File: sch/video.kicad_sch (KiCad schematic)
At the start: 14 parts

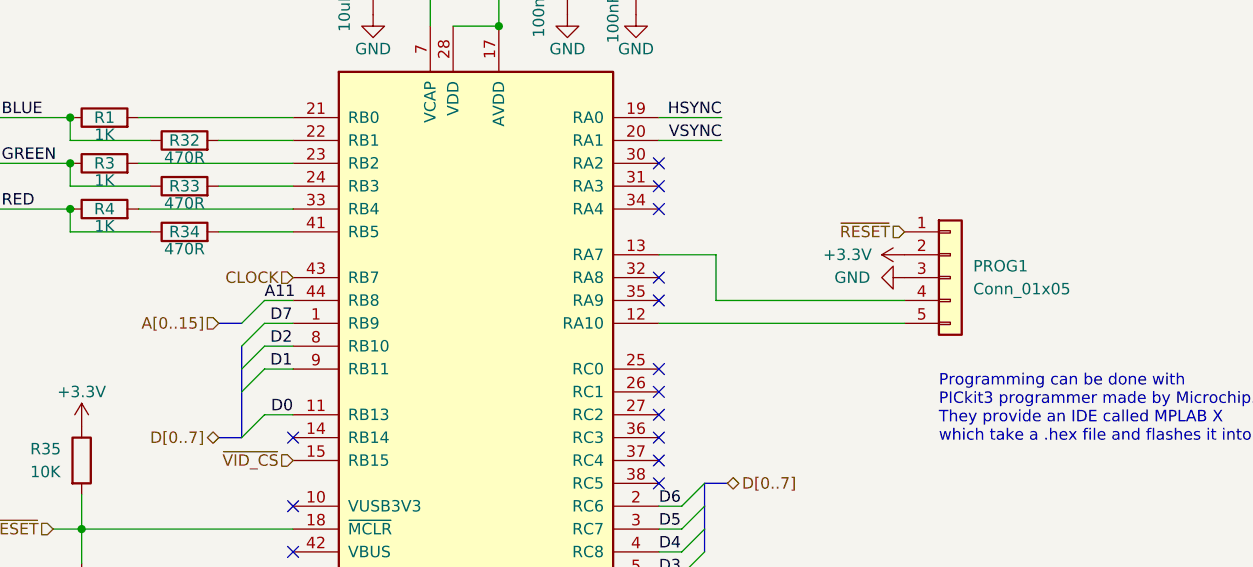
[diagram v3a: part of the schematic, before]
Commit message: bigger header pins
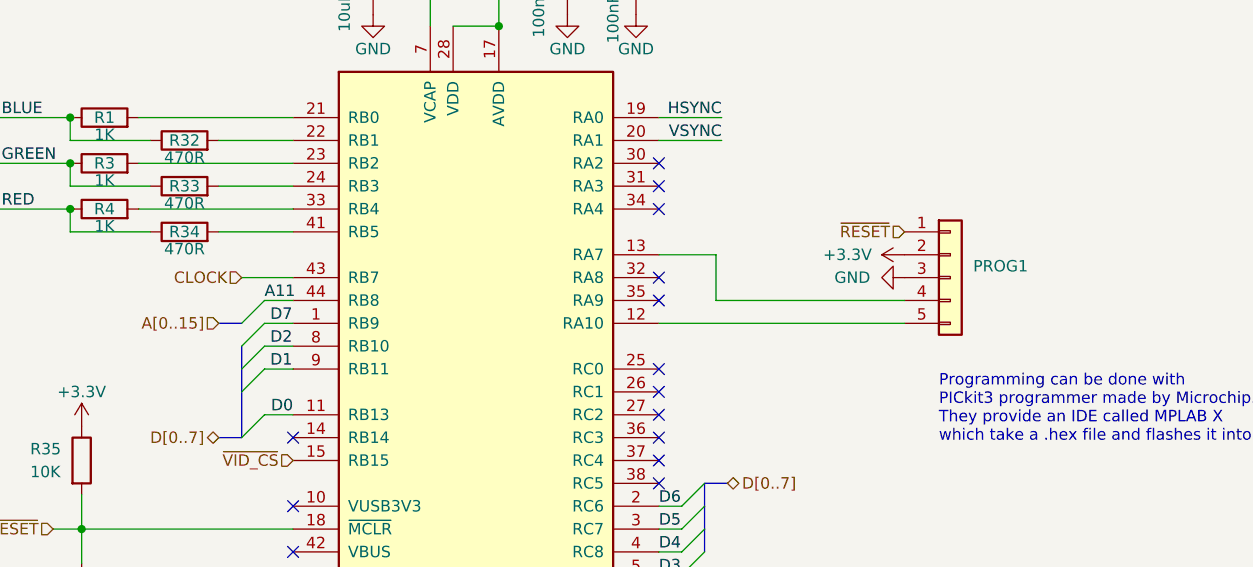
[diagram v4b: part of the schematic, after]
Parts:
- PROG1: value Conn_01x05 -> (none); footprint Connector_PinHeader_2.00mm:PinHeader_1x05_P2.00mm_Vertical -> (none)
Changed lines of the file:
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@@
+    (stroke (width 0) (type default) (color 0 0 0 0))
+  )
+  (wire (pts (xy 110.49 100.33) (xy 116.205 100.33))
     (stroke (width 0) (type default) (color 0 0 0 0))
   )
@@
     (effects (font (size 1.27 1.27)) (justify left bottom))
   )
-  (hierarchical_label "CLOCK" (shape input) (at 116.205 100.33 180)
+  (hierarchical_label "CLOCK" (shape input) (at 110.49 100.33 180)
     (effects (font (size 1.27 1.27)) (justify right))
   )
@@
       (effects (font (size 1.27 1.27)) (justify left))
     )
-    (property "Value" "Conn_01x05" (id 1) (at 191.77 101.5999 0)
-      (effects (font (size 1.27 1.27)) (justify left))
-    )
-    (property "Footprint" "Connector_PinHeader_2.00mm:PinHeader_1x05_P2.00mm_Vertical" (id 2) (at 189.23 100.33 0)
-      (effects (font (size 1.27 1.27)) hide)
-    )
+    (property "Value" "" (id 1) (at 191.77 101.5999 0)
+      (effects (font (size 1.27 1.27)) (justify left))
+    )
+    (property "Footprint" "" (id 2) (at 189.23 100.33 0)
+      (effects (font (size 1.27 1.27)) hide)
+    )

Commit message: small updates
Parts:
- PROG1: value (none) -> Conn_01x05; footprint (none) -> Connector_PinHeader_2.54mm:PinHeader_1x05_P2.54mm_Vertical
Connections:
- net ~{RESET} renamed ~{MCLR}
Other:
- note added: "Video will be generated using a microcontroller which is fast enough to generate the VGA timing signals. CPU will send a single byte to the MCU which can be be a char code or index of glyph, and the MCU just generates the video signal. This setup is limited in generating graphics but it avoids having to keep a large framebuffer in system memory."
- note removed: "Video will be generated using a microcontroller which is fast enough to generate the VGA timing signals. CPU will send a single byte to the MCU which can be be a char code or index of glyph, and the MCU just generates the video signal. This setup is limited in generating graphics but it avoids having to keep a large framebuffer."
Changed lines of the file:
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@@
-    (stroke (width 0) (type default) (color 0 0 0 0))
-  )
-  (wire (pts (xy 89.535 128.27) (xy 92.71 128.27))
     (stroke (width 0) (type default) (color 0 0 0 0))
   )
@@
     (stroke (width 0) (type default) (color 0 0 0 0))
   )
+  (wire (pts (xy 178.435 95.25) (xy 184.15 95.25))
+    (stroke (width 0) (type default) (color 0 0 0 0))
+  )
   (wire (pts (xy 80.645 80.01) (xy 80.645 74.93))
     (stroke (width 0) (type default) (color 0 0 0 0))
@@
   (wire (pts (xy 146.685 63.5) (xy 154.305 63.5))
     (stroke (width 0) (type default) (color 0 0 0 0))
+  )
+  (text "Video Controller" (at 31.75 26.035 0)
+    (effects (font (size 2 2) (thickness 0.254) bold) (justify left bottom))
   )
   (text "0x4800 - 0x480F" (at 31.75 28.575 0)
@@
     (effects (font (size 1.27 1.27)) (justify left bottom))
   )
-  (text "Video will be generated using a \nmicrocontroller which is fast enough to \ngenerate the VGA timing signals.\n\nCPU will send a single byte to the MCU which can\nbe be a char code or index of glyph, and the MCU\njust generates the video signal.\n\nThis setup is limited in generating graphics but\nit avoids having to keep a large framebuffer."
-    (at 31.75 52.705 0)
-    (effects (font (size 1.27 1.27)) (justify left bottom))
-  )
-  (text "Video Controller" (at 31.75 25.4 0)
-    (effects (font (size 2 2) (thickness 0.4) bold) (justify left bottom))
+  (text "Video will be generated using a \nmicrocontroller which is fast enough to \ngenerate the VGA timing signals.\n\nCPU will send a single byte to the MCU which can\nbe be a char code or index of glyph, and the MCU\njust generates the video signal.\n\nThis setup is limited in generating graphics but\nit avoids having to keep a large framebuffer\nin system memory."
+    (at 31.75 53.975 0)
+    (effects (font (size 1.27 1.27)) (justify left bottom))
   )
   (label "RED" (at 83.82 92.71 0)
@@
     (effects (font (size 1.27 1.27)) (justify left bottom))
   )
+  (label "~{MCLR}" (at 100.965 128.27 0)
+    (effects (font (size 1.27 1.27)) (justify left bottom))
+  )
   (label "VSYNC" (at 163.83 85.09 180)
     (effects (font (size 1.27 1.27)) (justify right bottom))
@@
     (effects (font (size 1.27 1.27)) (justify left bottom))
   )
+  (label "~{MCLR}" (at 178.435 95.25 0)
+    (effects (font (size 1.27 1.27)) (justify left bottom))
+  )
   (hierarchical_label "CLOCK" (shape input) (at 110.49 100.33 180)
     (effects (font (size 1.27 1.27)) (justify right))
@@
   (hierarchical_label "D[0..7]" (shape bidirectional) (at 164.465 123.19 0)
     (effects (font (size 1.27 1.27)) (justify left))
-  )
-  (hierarchical_label "~{RESET}" (shape input) (at 89.535 128.27 180)
-    (effects (font (size 1.27 1.27)) (justify right))
-  )
-  (hierarchical_label "~{RESET}" (shape input) (at 184.15 95.25 180)
-    (effects (font (size 1.27 1.27)) (justify right))
   )
   (hierarchical_label "A[0..15]" (shape input) (at 107.95 105.41 180)
@@
       (effects (font (size 1.27 1.27)) (justify left))
     )
-    (property "Value" "" (id 1) (at 191.77 101.5999 0)
-      (effects (font (size 1.27 1.27)) (justify left))
-    )
-    (property "Footprint" "" (id 2) (at 189.23 100.33 0)
-      (effects (font (size 1.27 1.27)) hide)
-    )
+    (property "Value" "Conn_01x05" (id 1) (at 191.77 101.5999 0)
+      (effects (font (size 1.27 1.27)) (justify left))
+    )
+    (property "Footprint" "Connector_PinHeader_2.54mm:PinHeader_1x05_P2.54mm_Vertical" (id 2) (at 189.23 100.33 0)
+      (effects (font (size 1.27 1.27)) hide)
+    )

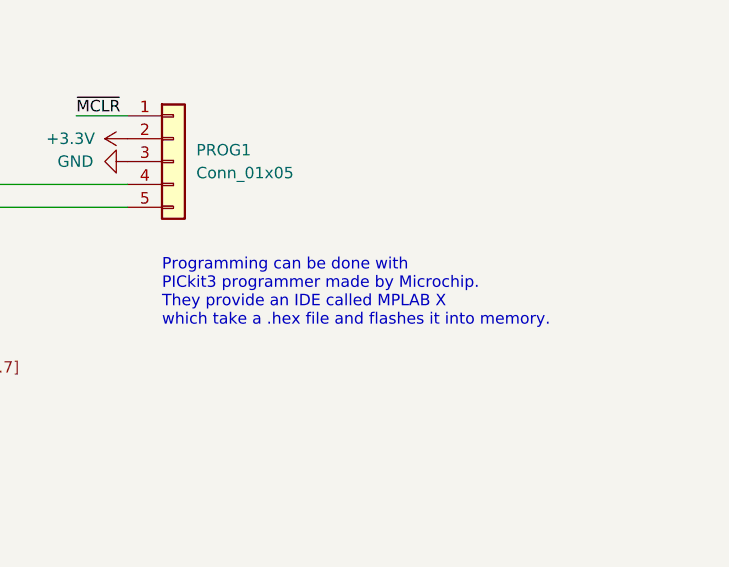
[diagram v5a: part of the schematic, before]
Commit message: Comments in Sch
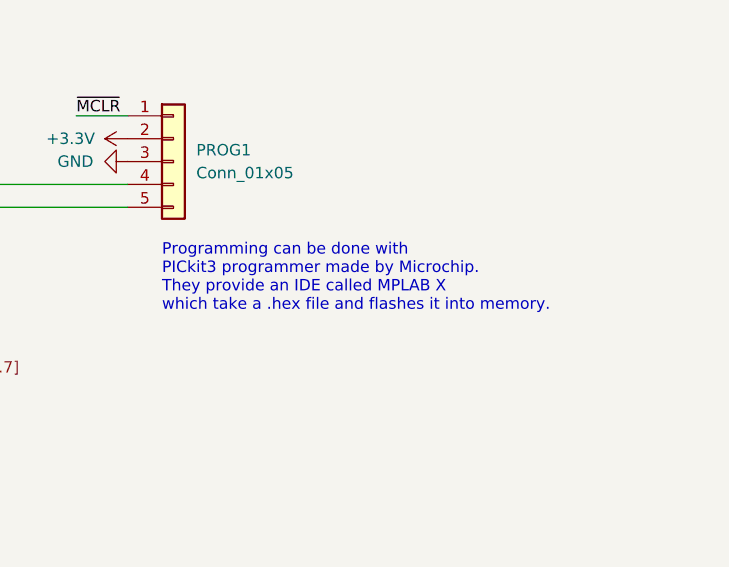
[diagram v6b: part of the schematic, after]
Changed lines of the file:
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@@
     (rev "1.0")
     (company "zrthxn")
+    (comment 1 "https://github.com/zrthxn/8puter")
+    (comment 2 "Open Source Hardware Project")
+    (comment 3 "Homebrew 8-Bit Computer")
   )
   (junction (at 80.645 74.93) (diameter 0) (color 0 0 0 0)
@@
   )
   (text "Programming can be done with\nPICkit3 programmer made by Microchip.\nThey provide an IDE called MPLAB X\nwhich take a .hex file and flashes it into memory."
-    (at 187.96 118.745 0)
+    (at 187.96 117.094 0)
     (effects (font (size 1.27 1.27)) (justify left bottom))
   )

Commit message: nicer label
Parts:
- VGA1: value DB15_Female_HighDensity -> (none); footprint Connector_Dsub:DSUB-15-HD_Female_Horizontal_P2.29x1.98mm_EdgePinOffset3.03mm_Housed_MountingHolesOffset4.94mm -> (none)
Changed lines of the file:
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@@
     (in_bom yes) (on_board yes)
     (property "Reference" "VGA1" (id 0) (at 70.485 62.23 0))
-    (property "Value" "DB15_Female_HighDensity" (id 1) (at 70.485 64.77 0))
-    (property "Footprint" "Connector_Dsub:DSUB-15-HD_Female_Horizontal_P2.29x1.98mm_EdgePinOffset3.03mm_Housed_MountingHolesOffset4.94mm" (id 2) (at 94.615 92.71 0)
+    (property "Value" "" (id 1) (at 70.485 64.77 0))
+    (property "Footprint" "" (id 2) (at 94.615 92.71 0)
       (effects (font (size 1.27 1.27)) hide)
     )

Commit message: improve routing
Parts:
- VGA1: value (none) -> DB15_Female_HighDensity; footprint (none) -> Connector_Dsub:DSUB-15-HD_Female_Horizontal_P2.29x1.98mm_EdgePinOffset3.03mm_Housed_MountingHolesOffset4.94mm
